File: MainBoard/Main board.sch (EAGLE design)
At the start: 10 parts

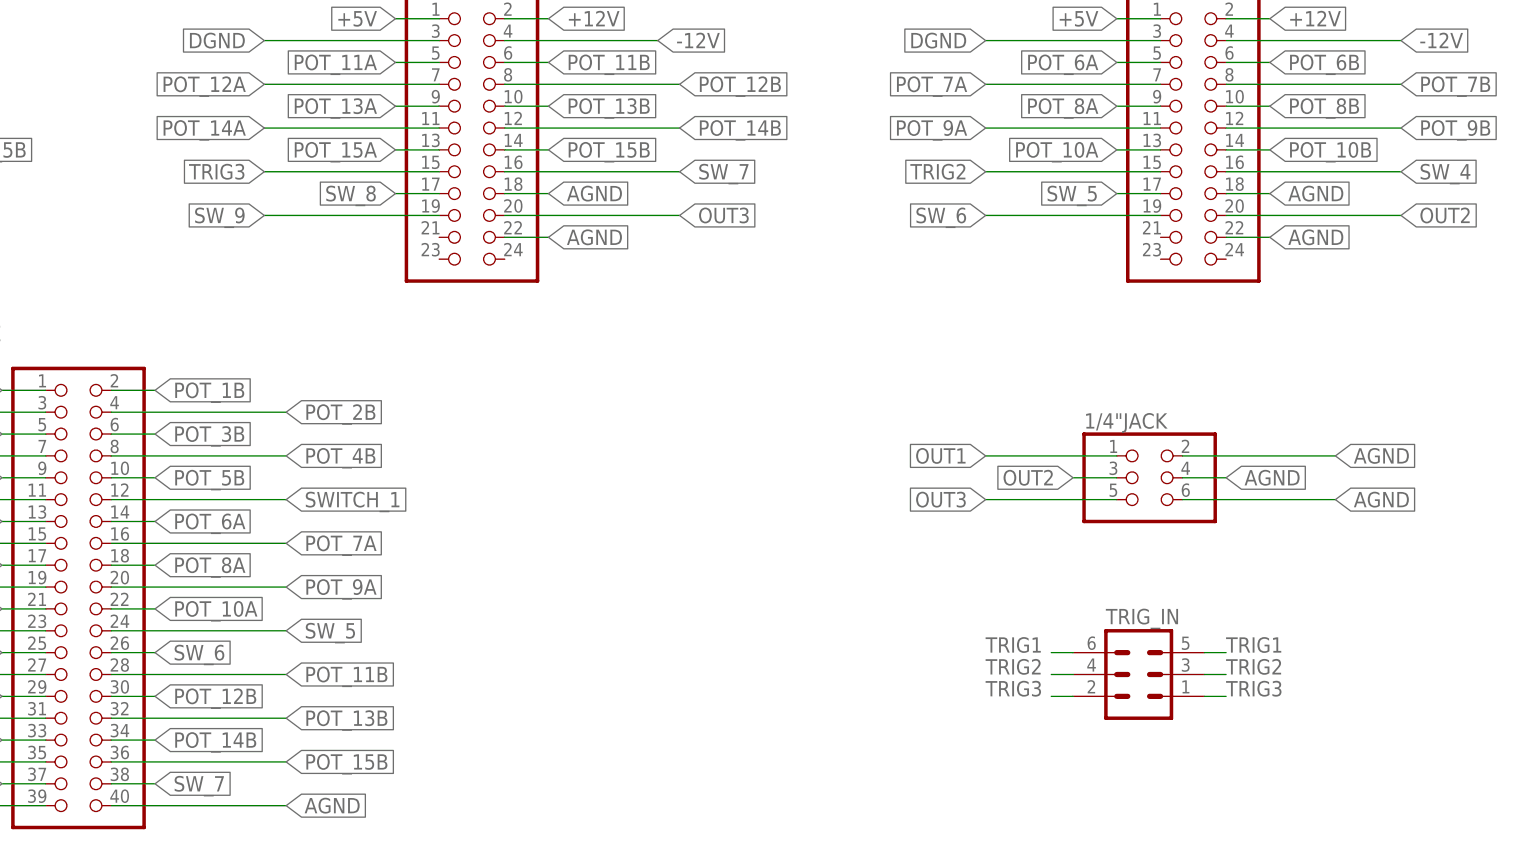
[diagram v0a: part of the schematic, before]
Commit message: Added silk screen
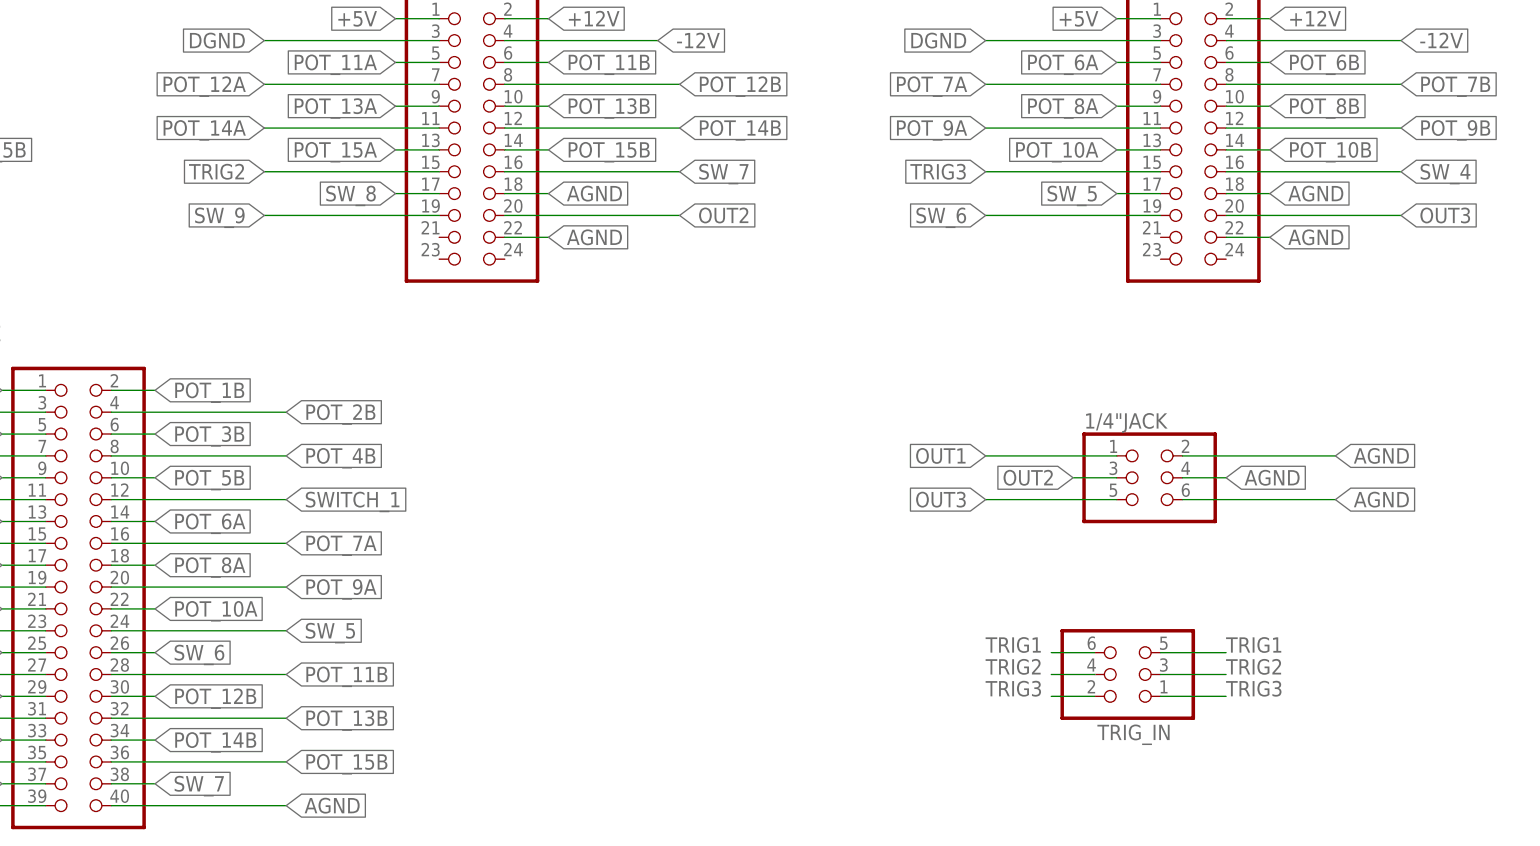
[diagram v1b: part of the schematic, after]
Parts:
- TRIG_IN: device con-lstb:MA03-2 -> pinhead:PINHD-2X3
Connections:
- net OUT2: now also INSTRUMENT_2.20; no longer INSTRUMENT_3.20
- net OUT3: now also INSTRUMENT_3.20; no longer INSTRUMENT_2.20
- net TRIG2: now also INSTRUMENT_2.15; no longer INSTRUMENT_3.15
- net TRIG3: now also INSTRUMENT_3.15; no longer INSTRUMENT_2.15
